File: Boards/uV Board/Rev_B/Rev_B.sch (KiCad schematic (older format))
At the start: 2 parts

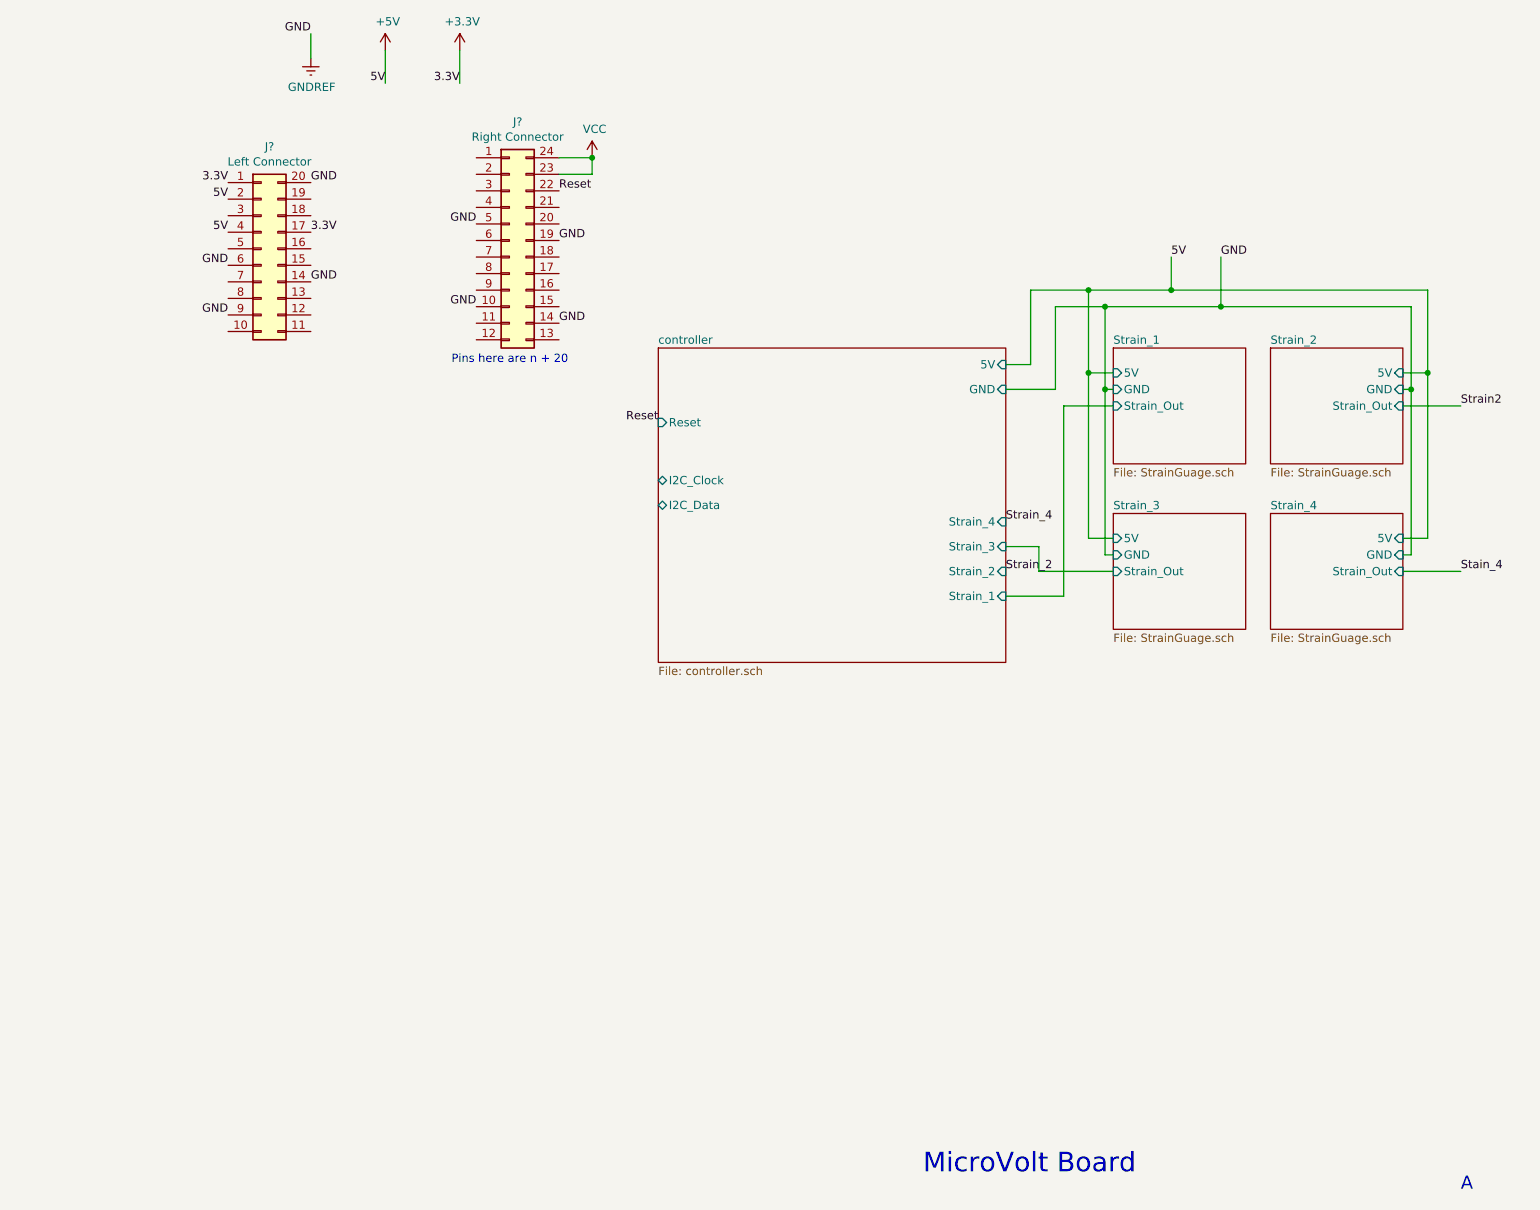
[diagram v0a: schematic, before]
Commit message: Created analog in sheets on ADC board, populated them, and connected them to controller.  Defined Interconnect pins. Placed mounting holes.
Converted some strain gauge connections to nets.
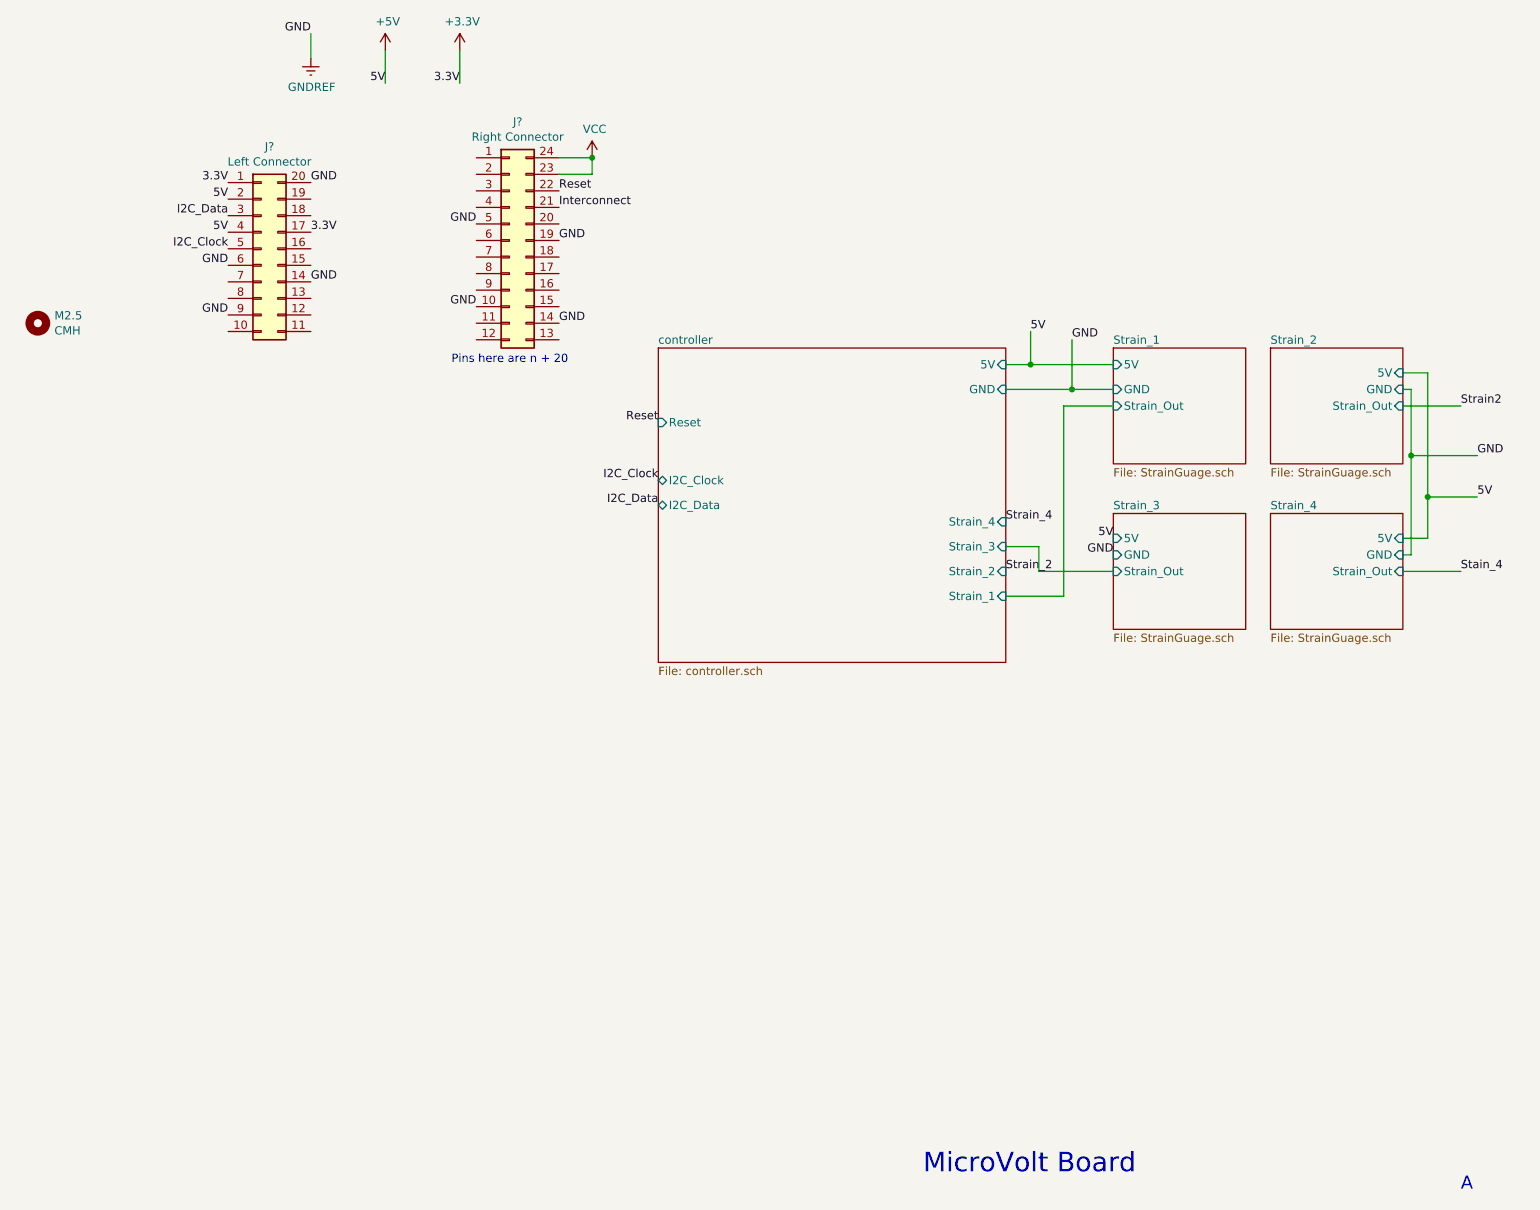
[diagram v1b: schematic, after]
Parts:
- added M2.5: CMH, symbol Mechanical:MountingHole
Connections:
- net Interconnect: now reaches J?.21 (Pin_21)
- net I2C_Data: now reaches J?.3 (Pin_3)
- net I2C_Clock: now reaches J?.5 (Pin_5)
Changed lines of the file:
@@
 F10 "I2C_Data" B L 5750 3500 50
-$EndSheet
-$Sheet
-S 8500 2550 800  700
-U 614FDE40
-F0 "Strain_1" 50
-F1 "StrainGuage.sch" 50
-F2 "5V" I L 8500 2700 50
-F3 "GND" I L 8500 2800 50
-F4 "Strain_Out" I L 8500 2900 50
 $EndSheet
 Text Notes 4500 2650 0    50   ~ 0
@@
 $EndSheet
 Wire Wire Line
-	8500 3700 8350 3700
-Wire Wire Line
-	8350 3700 8350 2700
-Wire Wire Line
-	8350 2700 8500 2700
-Wire Wire Line
 	10250 2700 10400 2700
 Wire Wire Line
-	10400 2700 10400 3700
+	10400 2700 10400 3450
 Wire Wire Line
 	10400 3700 10250 3700
-Text Label 8850 2000 0    50   ~ 0
+Text Label 8000 2450 0    50   ~ 0
 5V
-Text Label 9150 2000 0    50   ~ 0
+Text Label 8250 2500 0    50   ~ 0
 GND
 Wire Wire Line
-	8350 2700 8350 2200
+	8000 2650 8000 2450
 Wire Wire Line
-	8350 2200 8850 2200
-Connection ~ 8350 2700
-Wire Wire Line
-	10400 2700 10400 2200
-Wire Wire Line
-	10400 2200 8850 2200
-Wire Wire Line
-	8850 2200 8850 2000
-Connection ~ 10400 2700
-Wire Wire Line
-	8500 2800 8450 2800
-Wire Wire Line
-	8450 2800 8450 2300
-Wire Wire Line
-	8450 2300 9150 2300
-Wire Wire Line
-	9150 2300 9150 2000
-Wire Wire Line
-	8500 3800 8450 3800
-Wire Wire Line
-	8450 3800 8450 2800
-Connection ~ 8450 2800
+	8250 2800 8250 2500
 Wire Wire Line
 	10250 3800 10300 3800
 Wire Wire Line
-	10300 3800 10300 2800
+	10300 3800 10300 3200
 Wire Wire Line
 	10300 2800 10250 2800
-Wire Wire Line
-	10300 2800 10300 2300
-Wire Wire Line
-	10300 2300 9150 2300
-Connection ~ 10300 2800
-Connection ~ 9150 2300
-Connection ~ 8850 2200
-Wire Wire Line
-	8350 2200 8000 2200
-Wire Wire Line
-	8000 2200 8000 2650
-Wire Wire Line
-	8000 2650 7850 2650
-Connection ~ 8350 2200
-Wire Wire Line
-	8450 2300 8150 2300
-Wire Wire Line
-	8150 2300 8150 2800
-Wire Wire Line
-	8150 2800 7850 2800
-Connection ~ 8450 2300
 Wire Wire Line
 	8500 2900 8200 2900
@@
 Text Label 5750 3000 2    50   ~ 0
 Reset
+$Sheet
+S 8500 2550 800  700
+U 614FDE40
+F0 "Strain_1" 50
+F1 "StrainGuage.sch" 50
+F2 "5V" I L 8500 2650 50
+F3 "GND" I L 8500 2800 50
+F4 "Strain_Out" I L 8500 2900 50
+$EndSheet
+Wire Wire Line
+	7850 2650 8000 2650
+Connection ~ 8000 2650
+Wire Wire Line
+	8000 2650 8500 2650
+Connection ~ 8250 2800
+Wire Wire Line
+	8250 2800 8500 2800
+Wire Wire Line
+	7850 2800 8250 2800
+Text Label 8500 3700 2    50   ~ 0
+5V
+Text Label 8500 3800 2    50   ~ 0
+GND
+Text Label 10700 3200 0    50   ~ 0
+GND
+Text Label 10700 3450 0    50   ~ 0
+5V
+Wire Wire Line
+	10700 3200 10300 3200
+Connection ~ 10300 3200
+Wire Wire Line
+	10300 3200 10300 2800
+Wire Wire Line
+	10700 3450 10400 3450
+Connection ~ 10400 3450
+Wire Wire Line
+	10400 3450 10400 3700
+Text Label 3150 1950 2    50   ~ 0
+I2C_Clock
+Text Label 3150 1750 2    50   ~ 0
+I2C_Data
+Text Label 5750 3350 2    50   ~ 0
+I2C_Clock
+Text Label 5750 3500 2    50   ~ 0
+I2C_Data
+Text Label 5150 1700 0    50   ~ 0
+Interconnect
+$Comp
+L Mechanical:MountingHole M2.5
+U 1 1 615FF776
+P 2000 2400
+F 0 "M2.5" H 2100 2446 50  0000 L CNN
+F 1 "CMH" H 2100 2355 50  0000 L CNN
+F 2 "" H 2000 2400 50  0001 C CNN
+F 3 "~" H 2000 2400 50  0001 C CNN
+	1    2000 2400
+	1    0    0    -1
+$EndComp
 $EndSCHEMATC

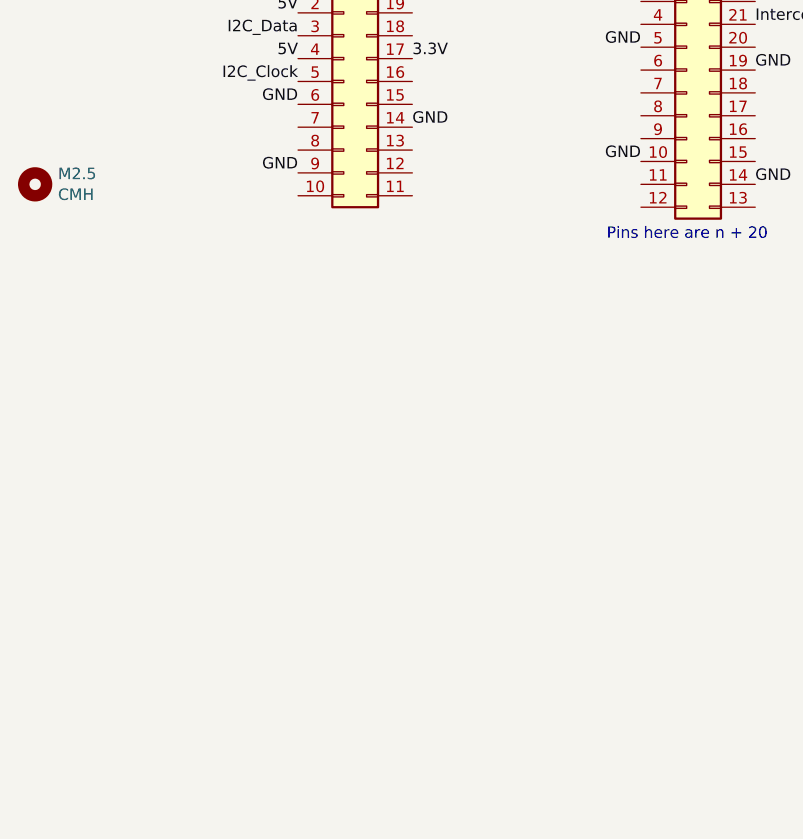
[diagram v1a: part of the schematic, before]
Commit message: Added regulator to ADC and micro boards. Added actual connectors for the strain gauge modules.
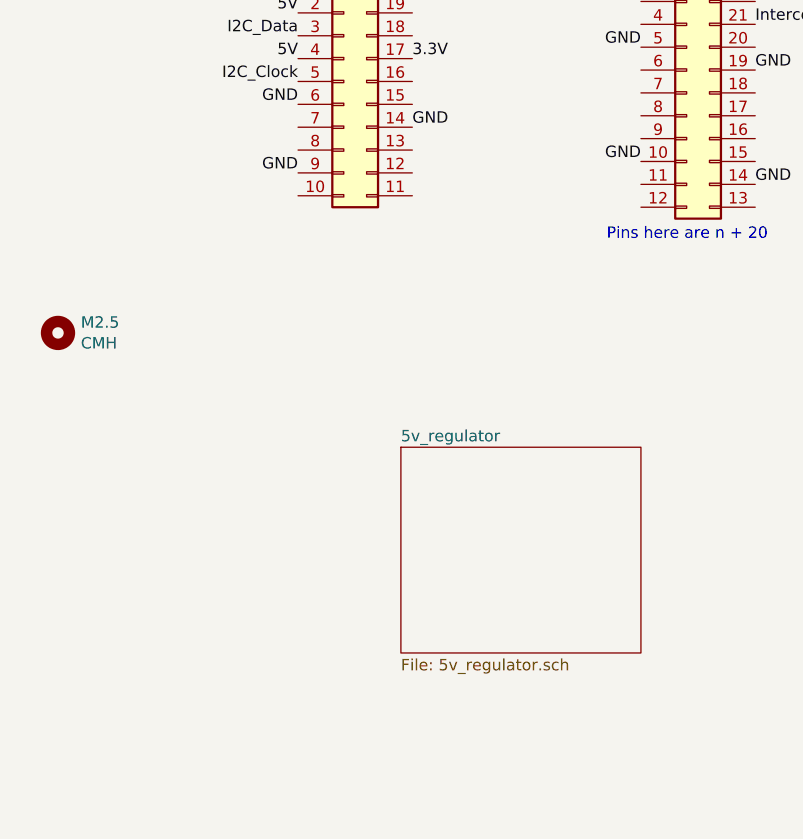
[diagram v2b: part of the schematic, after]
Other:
- moved on the sheet: M2.5
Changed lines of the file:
@@
 $Descr A4 11693 8268
 encoding utf-8
-Sheet 1 6
+Sheet 1 7
 Title ""
 Date ""
@@
 L Mechanical:MountingHole M2.5
 U 1 1 615FF776
-P 2000 2400
-F 0 "M2.5" H 2100 2446 50  0000 L CNN
-F 1 "CMH" H 2100 2355 50  0000 L CNN
-F 2 "" H 2000 2400 50  0001 C CNN
-F 3 "~" H 2000 2400 50  0001 C CNN
-	1    2000 2400
-	1    0    0    -1
-$EndComp
+P 2100 3050
+F 0 "M2.5" H 2200 3096 50  0000 L CNN
+F 1 "CMH" H 2200 3005 50  0000 L CNN
+F 2 "" H 2100 3050 50  0001 C CNN
+F 3 "~" H 2100 3050 50  0001 C CNN
+	1    2100 3050
+	1    0    0    -1
+$EndComp
+$Sheet
+S 3600 3550 1050 900
+U 616005C4
+F0 "5v_regulator" 50
+F1 "5v_regulator.sch" 50
+$EndSheet
 $EndSCHEMATC

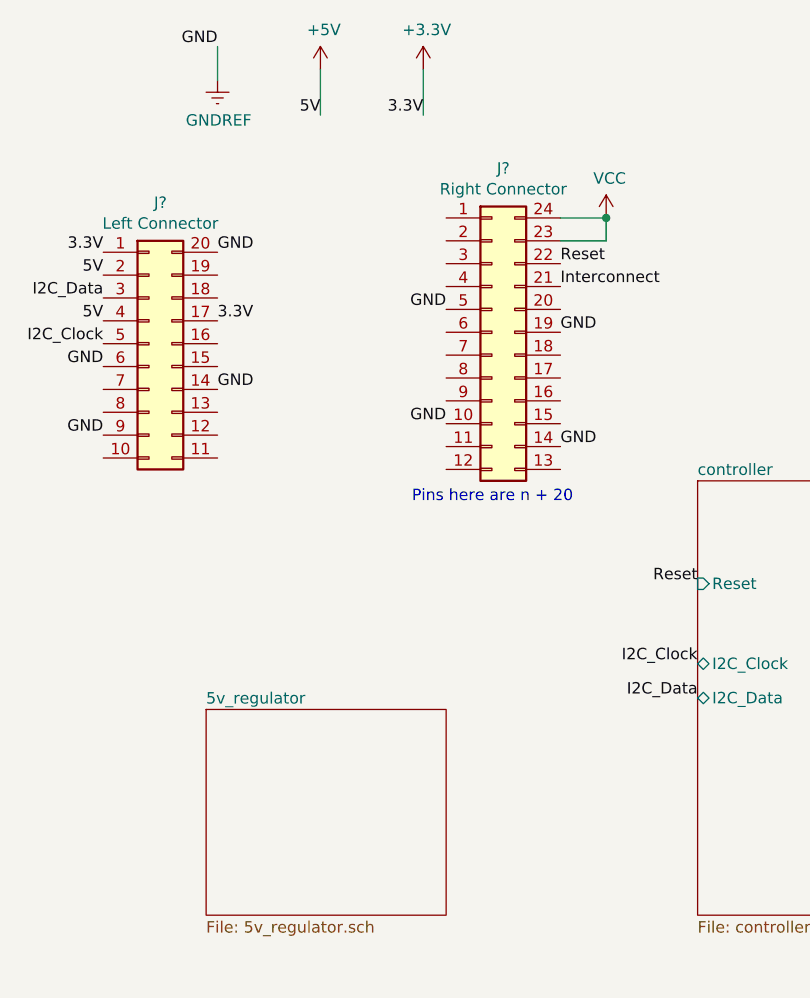
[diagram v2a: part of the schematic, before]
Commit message: Connected power regulator to ADC and micro boards. Added no connects to headers on ADC board. Preformed some footprinting operations on ADC board.
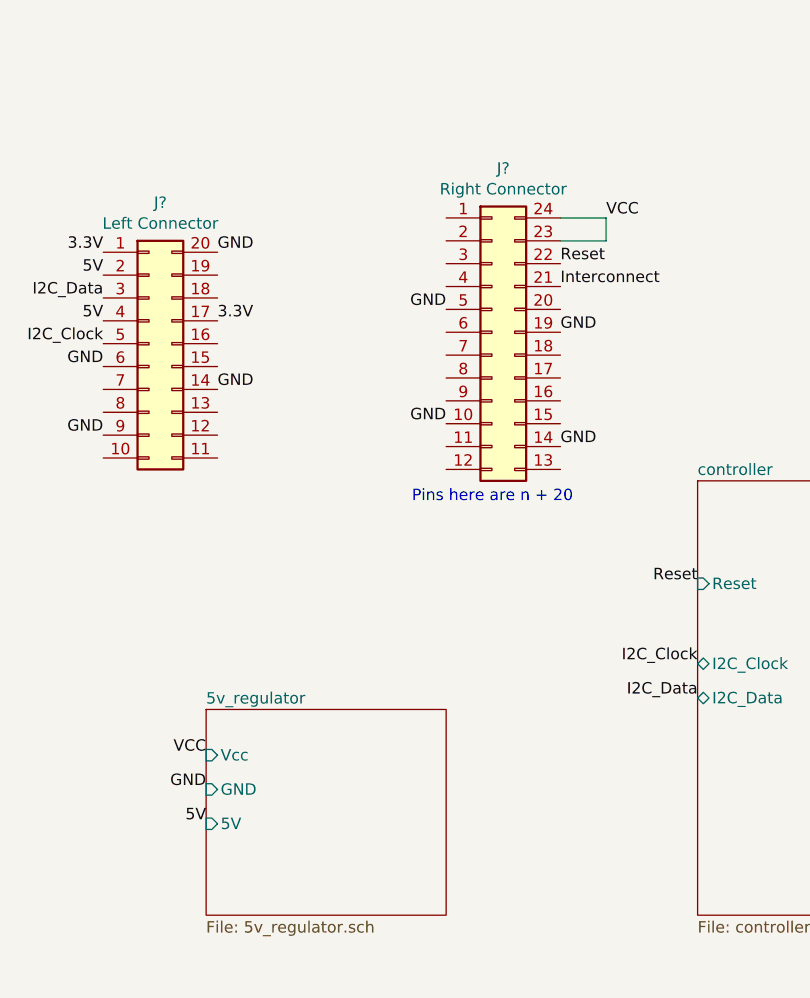
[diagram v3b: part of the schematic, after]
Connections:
- net +3V3 renamed 3.3V
- net +5V renamed 5V
- net GNDREF renamed GND
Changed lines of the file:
@@
 	1    0    0    -1
 $EndComp
-$Comp
-L power:VCC #PWR?
-U 1 1 614DBB26
-P 5350 1400
-F 0 "#PWR?" H 5350 1250 50  0001 C CNN
-F 1 "VCC" H 5365 1573 50  0000 C CNN
-F 2 "" H 5350 1400 50  0001 C CNN
-F 3 "" H 5350 1400 50  0001 C CNN
-	1    5350 1400
-	1    0    0    -1
-$EndComp
 Wire Wire Line
 	5350 1400 5150 1400
@@
 Wire Wire Line
 	5350 1500 5150 1500
-Connection ~ 5350 1400
 Text Label 5150 2400 0    50   ~ 0
 GND
@@
 Text Label 3150 1550 2    50   ~ 0
 3.3V
-$Comp
-L power:GNDREF #PWR?
-U 1 1 614F8C33
-P 3650 800
-F 0 "#PWR?" H 3650 550 50  0001 C CNN
-F 1 "GNDREF" H 3655 627 50  0000 C CNN
-F 2 "" H 3650 800 50  0001 C CNN
-F 3 "" H 3650 800 50  0001 C CNN
-	1    3650 800
-	1    0    0    -1
-$EndComp
-Text Label 3650 650  2    50   ~ 0
-GND
-Wire Wire Line
-	3650 650  3650 800
-$Comp
-L power:+3.3V #PWR?
-U 1 1 614FB62C
-P 4550 750
-F 0 "#PWR?" H 4550 600 50  0001 C CNN
-F 1 "+3.3V" H 4565 923 50  0000 C CNN
-F 2 "" H 4550 750 50  0001 C CNN
-F 3 "" H 4550 750 50  0001 C CNN
-	1    4550 750
-	1    0    0    -1
-$EndComp
-Text Label 4550 950  2    50   ~ 0
-3.3V
-Wire Wire Line
-	4550 950  4550 750
-$Comp
-L power:+5V #PWR?
-U 1 1 614FCDE4
-P 4100 750
-F 0 "#PWR?" H 4100 600 50  0001 C CNN
-F 1 "+5V" H 4115 923 50  0000 C CNN
-F 2 "" H 4100 750 50  0001 C CNN
-F 3 "" H 4100 750 50  0001 C CNN
-	1    4100 750
-	1    0    0    -1
-$EndComp
-Text Label 4100 950  2    50   ~ 0
-5V
-Wire Wire Line
-	4100 950  4100 750
 $Sheet
 S 5750 2550 2100 1900
@@
 F0 "5v_regulator" 50
 F1 "5v_regulator.sch" 50
-$EndSheet
+F2 "Vcc" I L 3600 3750 50
+F3 "GND" I L 3600 3900 50
+F4 "5V" I L 3600 4050 50
+$EndSheet
+Text Label 5350 1400 0    50   ~ 0
+VCC
+Text Label 3600 3750 2    50   ~ 0
+VCC
+Text Label 3600 4050 2    50   ~ 0
+5V
+Text Label 3600 3900 2    50   ~ 0
+GND
 $EndSCHEMATC
